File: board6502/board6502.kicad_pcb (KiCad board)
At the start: 2 copper layers, 48 parts, among them J1 IO Pinheader, J2 UART, J3 USB_B, J4 Expansion Port, J5 Power connector, SW1 Reset button, SW2 SW_NMI, U1 DS1813, U2 74LS00, U3 74LS04, U4 W65C22N, U5 74LS30, U6 W65C51N, U7 W65C02, U8 AT28C64B, U9 CY7C199, X1 1-10MHz, Y1 1.8432M

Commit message: finally complete PCB routing
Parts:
- moved J5 112.2 mm to (102.0, 53.0), turned to 270 degrees
- moved J4 97.0 mm to (149.6, 136.8), turned to 270 degrees
- moved R8 94.8 mm to (121.8, 58.8), turned to 0 degrees
- moved R4 87.1 mm to (123.8, 68.8)
- moved R6 84.0 mm to (121.8, 65.4), turned to 0 degrees
- moved C10 83.9 mm to (155.2, 133.8), turned to 270 degrees
- moved D4 79.2 mm to (131.8, 55.8), turned to 90 degrees
- moved C3 78.9 mm to (132.2, 74.8), turned to 90 degrees
- moved R9 78.7 mm to (127.4, 55.8), turned to 90 degrees
- moved U4 77.6 mm to (186.8, 104.4), turned to 180 degrees
- moved U9 76.6 mm to (132.0, 128.8), turned to 180 degrees
- moved JP3 76.4 mm to (113.2, 72.8)
- moved C12 76.3 mm to (135.8, 54.6)
- moved Y1 76.1 mm to (192.1, 140.3), turned to 90 degrees
- moved X1 75.1 mm to (100.0, 58.8)
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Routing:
- net GND: track 6.24 -> 744.2 mm, vias 0 -> 5
- net +5V: track 2.07 -> 550.3 mm, vias 0 -> 6
- net _IRQ: track 0.00 -> 256.5 mm, vias 0 -> 3
- net D7: track 0.00 -> 229.8 mm, vias 0 -> 5
- net D6: track 0.00 -> 228.2 mm, vias 0 -> 4
- net _RESET: track 0.00 -> 223.9 mm, vias 0 -> 4
- net CLK: track 0.00 -> 208.2 mm, vias 0 -> 4
- net D5: track 0.00 -> 207.8 mm, vias 0 -> 4
- net D4: track 0.00 -> 199.1 mm, vias 0 -> 4
- net A4: track 0.00 -> 188.5 mm, vias 0 -> 7
- net D3: track 0.00 -> 186.3 mm, vias 0 -> 3
- net A7: track 0.00 -> 185.7 mm, vias 0 -> 2
- net RW_: track 0.00 -> 184.7 mm, vias 0 -> 1
- net A5: track 0.00 -> 176.2 mm, vias 0 -> 5
- net A12: track 0.00 -> 159.9 mm, vias 0 -> 4
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
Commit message: revisit power lines
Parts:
- moved C11 65.1 mm to (166.2, 119.4), turned to 90 degrees
- moved C3 17.0 mm to (131.0, 91.8), turned to 180 degrees
- moved C8 5.20 mm to (109.8, 88.0)
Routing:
- net GND: track 744.2 -> 623.6 mm, vias 5 -> 7
- net +5V: track 550.3 -> 507.5 mm, vias 6 -> 7
- net _IRQ: track 256.5 -> 243.0 mm
- net Net-(U3-Pad9): track 45.4 -> 39.4 mm, vias 0 -> 2
- net CLK: track 208.2 -> 205.1 mm
- net _RESET: track 223.9 -> 224.8 mm, vias 4 -> 5
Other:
- net class Power: trace_width 0.254 -> 0.508

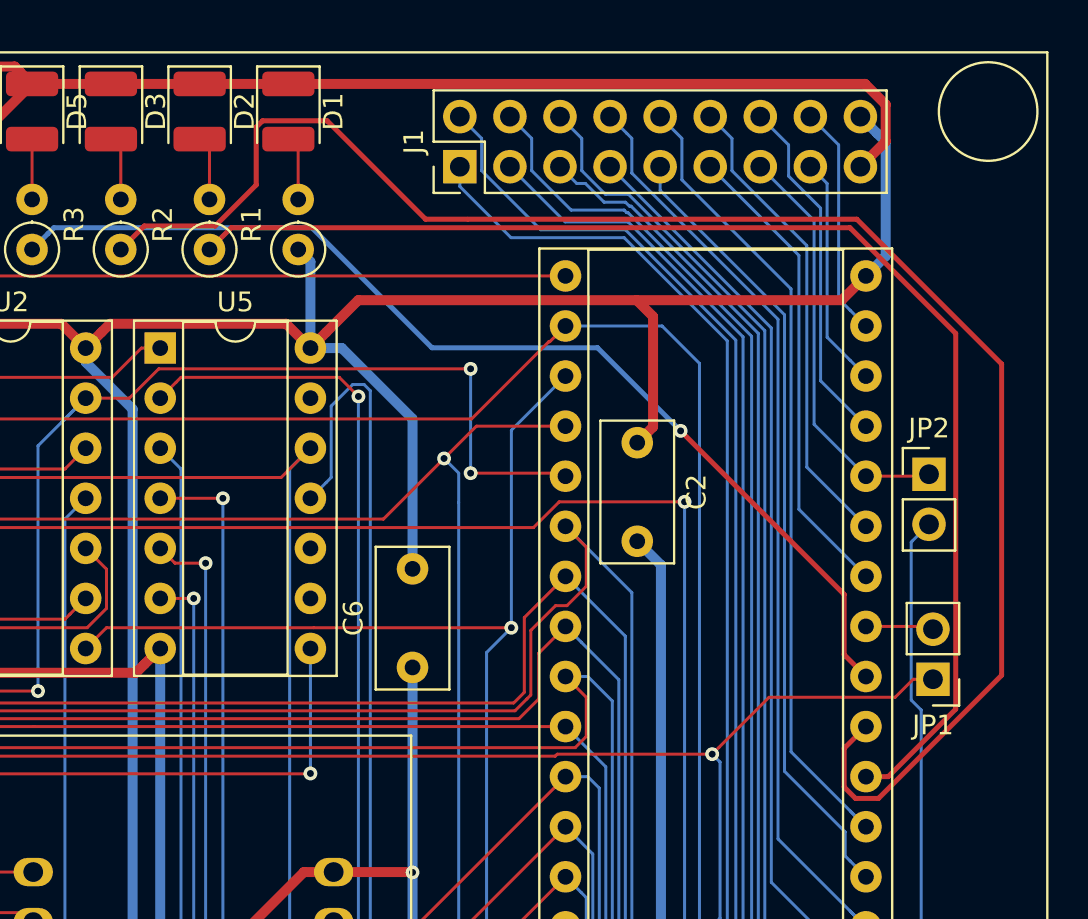
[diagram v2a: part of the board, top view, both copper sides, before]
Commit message: redo led traces
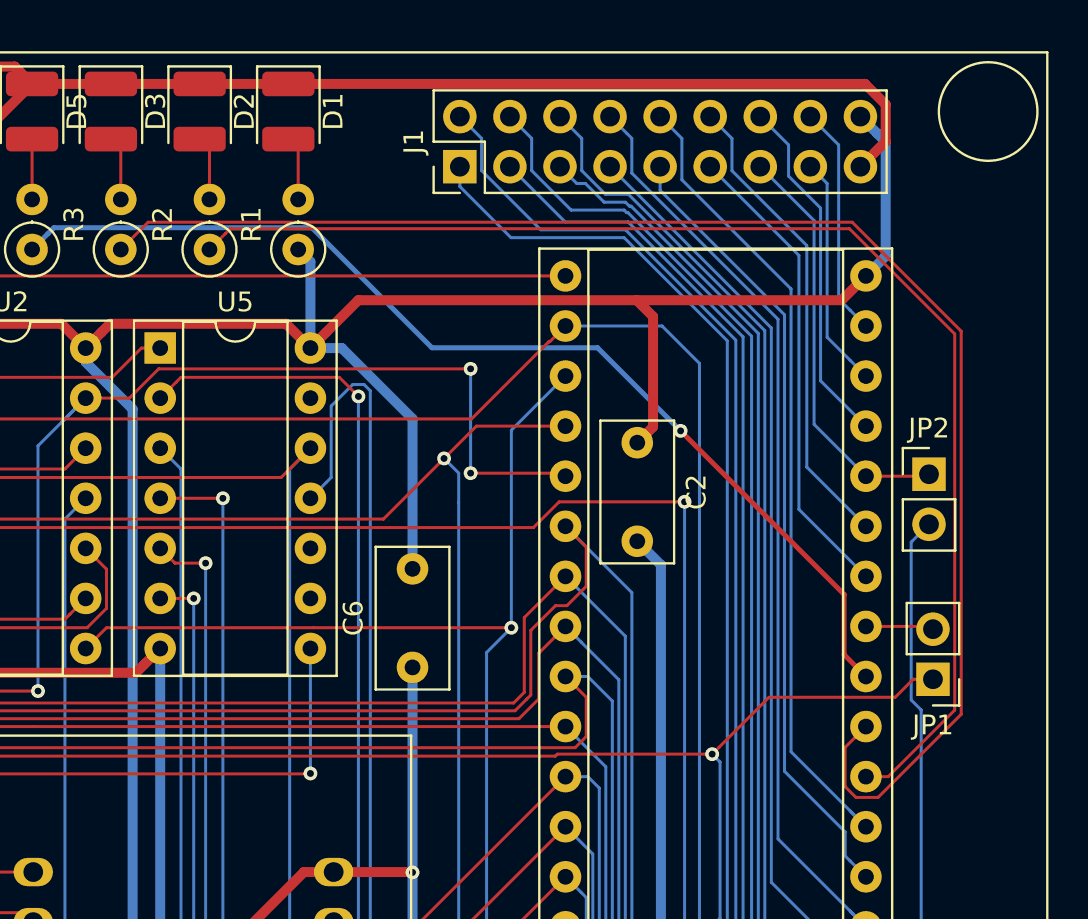
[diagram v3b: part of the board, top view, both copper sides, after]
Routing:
- net LED2: track 84.3 -> 76.3 mm
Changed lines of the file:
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@@
     (thickness 1.6)
     (drawings 7)
-    (tracks 1487)
+    (tracks 1480)
     (zones 0)
     (modules 48)
@@
     (add_net IO8)
     (add_net IO9)
+    (add_net LED1)
+    (add_net LED2)
+    (add_net LED3)
     (add_net "Net-(C1-Pad1)")
     (add_net "Net-(D1-Pad2)")
@@
     (add_net +5V)
     (add_net GND)
-    (add_net LED1)
-    (add_net LED2)
-    (add_net LED3)
+  )
+  (module Resistor_THT:R_Axial_DIN0207_L6.3mm_D2.5mm_P2.54mm_Vertical (layer F.Cu)
+    (at 153.5 54.8 90)
+    (descr "Resistor, Axial_DIN0207 series, Axial, Vertical, pin pitch=2.54mm, 0.25W = 1/4W, length*diameter=6.3*2.5mm^2, http://cdn-reichelt.de/documents/datenblatt/B400/1_4W%23YAG.pdf")
+    (tags "Resistor Axial_DIN0207 series Axial Vertical pin pitch 2.54mm 0.25W = 1/4W length 6.3mm diameter 2.5mm")
+    (fp_text reference R2 (at 1.27 -2.37 90) (layer F.SilkS)
+      (effects (font (size 1 1) (thickness 0.15)))
+    )
+    (fp_text value 330 (at 1.27 2.37 90) (layer F.Fab)
+      (effects (font (size 1 1) (thickness 0.15)))
+    )
+    (fp_circle (center 0 0) (end 1.25 0) (layer F.Fab) (width 0.1))
+    (fp_circle (center 0 0) (end 1.37 0) (layer F.SilkS) (width 0.12))
+    (fp_line (start 0 0) (end 2.54 0) (layer F.Fab) (width 0.1))
+    (fp_line (start 1.37 0) (end 1.44 0) (layer F.SilkS) (width 0.12))
+    (fp_line (start -1.5 -1.5) (end -1.5 1.5) (layer F.CrtYd) (width 0.05))
+    (fp_line (start -1.5 1.5) (end 3.59 1.5) (layer F.CrtYd) (width 0.05))
+    (fp_line (start 3.59 1.5) (end 3.59 -1.5) (layer F.CrtYd) (width 0.05))
+    (fp_line (start 3.59 -1.5) (end -1.5 -1.5) (layer F.CrtYd) (width 0.05))
+    (fp_text user %R (at 1.27 -2.37 90) (layer F.Fab)
+      (effects (font (size 1 1) (thickness 0.15)))
+    )
+    (pad 1 thru_hole circle (at 0 0 90) (size 1.6 1.6) (drill 0.8) (layers *.Cu *.Mask)
+      (net 64 LED1))
+    (pad 2 thru_hole oval (at 2.54 0 90) (size 1.6 1.6) (drill 0.8) (layers *.Cu *.Mask)
+      (net 6 "Net-(D2-Pad2)"))
+    (model ${KISYS3DMOD}/Resistor_THT.3dshapes/R_Axial_DIN0207_L6.3mm_D2.5mm_P2.54mm_Vertical.wrl
+      (at (xyz 0 0 0))
+      (scale (xyz 1 1 1))
+      (rotate (xyz 0 0 0))
+    )
   )
   (module Package_DIP:DIP-28_W7.62mm_Socket (layer F.Cu)
@@
   )
   (module Resistor_THT:R_Axial_DIN0207_L6.3mm_D2.5mm_P2.54mm_Vertical (layer F.Cu)
-    (at 153.5 54.8 90)
-    (descr "Resistor, Axial_DIN0207 series, Axial, Vertical, pin pitch=2.54mm, 0.25W = 1/4W, length*diameter=6.3*2.5mm^2, http://cdn-reichelt.de/documents/datenblatt/B400/1_4W%23YAG.pdf")
-    (tags "Resistor Axial_DIN0207 series Axial Vertical pin pitch 2.54mm 0.25W = 1/4W length 6.3mm diameter 2.5mm")
-    (fp_text reference R2 (at 1.27 -2.37 90) (layer F.SilkS)
-      (effects (font (size 1 1) (thickness 0.15)))
-    )
-    (fp_text value 330 (at 1.27 2.37 90) (layer F.Fab)
-      (effects (font (size 1 1) (thickness 0.15)))
-    )
-    (fp_circle (center 0 0) (end 1.25 0) (layer F.Fab) (width 0.1))
-    (fp_circle (center 0 0) (end 1.37 0) (layer F.SilkS) (width 0.12))
-    (fp_line (start 0 0) (end 2.54 0) (layer F.Fab) (width 0.1))
-    (fp_line (start 1.37 0) (end 1.44 0) (layer F.SilkS) (width 0.12))
-    (fp_line (start -1.5 -1.5) (end -1.5 1.5) (layer F.CrtYd) (width 0.05))
-    (fp_line (start -1.5 1.5) (end 3.59 1.5) (layer F.CrtYd) (width 0.05))
-    (fp_line (start 3.59 1.5) (end 3.59 -1.5) (layer F.CrtYd) (width 0.05))
-    (fp_line (start 3.59 -1.5) (end -1.5 -1.5) (layer F.CrtYd) (width 0.05))
-    (fp_text user %R (at 1.27 -2.37 90) (layer F.Fab)
-      (effects (font (size 1 1) (thickness 0.15)))
-    )
-    (pad 1 thru_hole circle (at 0 0 90) (size 1.6 1.6) (drill 0.8) (layers *.Cu *.Mask)
-      (net 64 LED1))
-    (pad 2 thru_hole oval (at 2.54 0 90) (size 1.6 1.6) (drill 0.8) (layers *.Cu *.Mask)
-      (net 6 "Net-(D2-Pad2)"))
-    (model ${KISYS3DMOD}/Resistor_THT.3dshapes/R_Axial_DIN0207_L6.3mm_D2.5mm_P2.54mm_Vertical.wrl
-      (at (xyz 0 0 0))
-      (scale (xyz 1 1 1))
-      (rotate (xyz 0 0 0))
-    )
-  )
-  (module Resistor_THT:R_Axial_DIN0207_L6.3mm_D2.5mm_P2.54mm_Vertical (layer F.Cu)
     (at 149 54.8 90)
     (descr "Resistor, Axial_DIN0207 series, Axial, Vertical, pin pitch=2.54mm, 0.25W = 1/4W, length*diameter=6.3*2.5mm^2, http://cdn-reichelt.de/documents/datenblatt/B400/1_4W%23YAG.pdf")
@@
   (segment (start 112.9624 74.04) (end 113.2 73.8024) (width 0.1524) (layer F.Cu) (net 63))
   (segment (start 107.62 74.04) (end 112.9624 74.04) (width 0.1524) (layer F.Cu) (net 63))
-  (segment (start 154.604801 53.695199) (end 153.5 54.8) (width 0.254) (layer F.Cu) (net 64))
-  (segment (start 185.990305 53.695199) (end 154.604801 53.695199) (width 0.254) (layer F.Cu) (net 64))
-  (segment (start 187.93137 81.54) (end 191.354801 78.116569) (width 0.254) (layer F.Cu) (net 64))
-  (segment (start 191.354801 59.059695) (end 185.990305 53.695199) (width 0.254) (layer F.Cu) (net 64))
-  (segment (start 191.354801 78.116569) (end 191.354801 59.059695) (width 0.254) (layer F.Cu) (net 64))
-  (segment (start 186.8 81.54) (end 187.93137 81.54) (width 0.254) (layer F.Cu) (net 64))
-  (segment (start 155.87019 48.595188) (end 156.195188 48.27019) (width 0.254) (layer F.Cu) (net 65))
-  (segment (start 155.87019 51.524916) (end 155.87019 48.595188) (width 0.254) (layer F.Cu) (net 65))
-  (segment (start 153.788814 53.606292) (end 155.87019 51.524916) (width 0.254) (layer F.Cu) (net 65))
-  (segment (start 150.193708 53.606292) (end 153.788814 53.606292) (width 0.254) (layer F.Cu) (net 65))
-  (segment (start 149 54.8) (end 150.193708 53.606292) (width 0.254) (layer F.Cu) (net 65))
-  (segment (start 159.47019 48.27019) (end 164.463389 53.263389) (width 0.254) (layer F.Cu) (net 65))
-  (segment (start 156.195188 48.27019) (end 159.07019 48.27019) (width 0.254) (layer F.Cu) (net 65))
-  (segment (start 159.07019 48.27019) (end 159.47019 48.27019) (width 0.254) (layer F.Cu) (net 65))
-  (segment (start 164.463389 53.263389) (end 166.6 53.263389) (width 0.254) (layer F.Cu) (net 65))
-  (segment (start 193.684731 60.611509) (end 186.336611 53.263389) (width 0.254) (layer F.Cu) (net 65))
-  (segment (start 193.684731 76.39731) (end 193.684731 60.611509) (width 0.254) (layer F.Cu) (net 65))
-  (segment (start 187.437239 82.644801) (end 193.684731 76.39731) (width 0.254) (layer F.Cu) (net 65))
-  (segment (start 186.269695 82.644801) (end 187.437239 82.644801) (width 0.254) (layer F.Cu) (net 65))
-  (segment (start 185.695199 82.070305) (end 186.269695 82.644801) (width 0.254) (layer F.Cu) (net 65))
-  (segment (start 185.695199 80.104801) (end 185.695199 82.070305) (width 0.254) (layer F.Cu) (net 65))
-  (segment (start 186.8 79) (end 185.695199 80.104801) (width 0.254) (layer F.Cu) (net 65))
-  (segment (start 166.614747 53.263389) (end 186.336611 53.263389) (width 0.254) (layer F.Cu) (net 65))
+  (segment (start 154.554001 53.745999) (end 154.299999 54.000001) (width 0.1524) (layer F.Cu) (net 64))
+  (segment (start 154.299999 54.000001) (end 153.5 54.8) (width 0.1524) (layer F.Cu) (net 64))
+  (segment (start 185.965921 53.745999) (end 154.554001 53.745999) (width 0.1524) (layer F.Cu) (net 64))
+  (segment (start 191.304001 59.084079) (end 185.965921 53.745999) (width 0.1524) (layer F.Cu) (net 64))
+  (segment (start 191.304001 78.167369) (end 191.304001 59.084079) (width 0.1524) (layer F.Cu) (net 64))
+  (segment (start 187.93137 81.54) (end 191.304001 78.167369) (width 0.1524) (layer F.Cu) (net 64))
+  (segment (start 186.8 81.54) (end 187.93137 81.54) (width 0.1524) (layer F.Cu) (net 64))
+  (segment (start 186.102698 53.415789) (end 191.634211 58.947302) (width 0.1524) (layer F.Cu) (net 65))
+  (segment (start 150.384211 53.415789) (end 186.102698 53.415789) (width 0.1524) (layer F.Cu) (net 65))
+  (segment (start 149 54.8) (end 150.384211 53.415789) (width 0.1524) (layer F.Cu) (net 65))
+  (segment (start 185.745999 82.045921) (end 186.294079 82.594001) (width 0.1524) (layer F.Cu) (net 65))
+  (segment (start 186.294079 82.594001) (end 187.416197 82.594001) (width 0.1524) (layer F.Cu) (net 65))
+  (segment (start 185.745999 80.054001) (end 185.745999 82.045921) (width 0.1524) (layer F.Cu) (net 65))
+  (segment (start 186.8 79) (end 185.745999 80.054001) (width 0.1524) (layer F.Cu) (net 65))
+  (segment (start 191.634211 78.375987) (end 187.416197 82.594001) (width 0.1524) (layer F.Cu) (net 65))
+  (segment (start 191.634211 58.947302) (end 191.634211 78.375987) (width 0.1524) (layer F.Cu) (net 65))
   (segment (start 121.75 65.4) (end 122.314001 65.964001) (width 0.1524) (layer F.Cu) (net 66))
   (segment (start 113.84 85.58) (end 116.33021 83.08979) (width 0.1524) (layer B.Cu) (net 66))
@@
   (segment (start 145.299999 54.000001) (end 144.5 54.8) (width 0.254) (layer B.Cu) (net 68))
   (segment (start 145.604801 53.695199) (end 145.299999 54.000001) (width 0.254) (layer B.Cu) (net 68))
-  (segment (start 158.695199 53.695199) (end 145.604801 53.695199) (width 0.254) (layer B.Cu) (net 68))
   (segment (start 164.784801 59.784801) (end 158.695199 53.695199) (width 0.254) (layer B.Cu) (net 68))
   (segment (start 173.184801 59.784801) (end 164.784801 59.784801) (width 0.254) (layer B.Cu) (net 68))
   (segment (start 177.4 64) (end 173.184801 59.784801) (width 0.254) (layer B.Cu) (net 68))
+  (segment (start 158.695199 53.695199) (end 145.604801 53.695199) (width 0.254) (layer B.Cu) (net 68))
   (segment (start 148.274001 73.985999) (end 158.794001 73.985999) (width 0.1524) (layer F.Cu) (net 69))
   (segment (start 147.22 75.04) (end 148.274001 73.985999) (width 0.1524) (layer F.Cu) (net 69))

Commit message: satisfy design rules
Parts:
- moved J5 53.7 mm to (50.2, 39.0)
- moved C12 52.9 mm to (84.8, 40.6)
- moved C6 52.9 mm to (112.8, 62.0)
- moved U8 52.9 mm to (108.8, 105.4)
- moved C1 52.9 mm to (141.0, 111.8)
- moved C3 52.9 mm to (80.0, 77.8)
- moved C5 52.9 mm to (67.4, 59.8)
- moved C7 52.9 mm to (131.6, 101.2)
- moved C8 52.9 mm to (58.8, 74.0)
- moved D1 52.9 mm to (106.5, 33.8)
- moved D2 52.9 mm to (102.0, 33.8)
- moved D3 52.9 mm to (97.5, 33.8)
- moved D5 52.9 mm to (93.5, 33.8)
- moved J2 52.9 mm to (141.0, 95.0)
- moved J3 52.9 mm to (59.5, 38.8)
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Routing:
- net GND: track 623.6 -> 625.7 mm
- net +5V: track 507.5 -> 508.5 mm
- net _RESET: track 224.8 -> 225.4 mm
- net _NMI: track 128.4 -> 127.8 mm
- net D5: track 207.8 -> 208.4 mm
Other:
- board outline added: 100 x 100 mm
